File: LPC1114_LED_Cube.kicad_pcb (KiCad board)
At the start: 2 copper layers, 100 x 100 mm, 88 parts, among them Q201 BSS138, Q202 BSS138, Q203 BSS138, Q204 BSS138, Q205 IRLML6402TRPBF, Q206 IRLML6402TRPBF, Q207 IRLML6402TRPBF, Q208 IRLML6402TRPBF, Q209 BSS138, Q210 BSS138, Q211 BSS138, Q212 BSS138, Q213 IRLML6402TRPBF, Q214 IRLML6402TRPBF, Q215 IRLML6402TRPBF, Q216 IRLML6402TRPBF, Y101 12MHZ, Y102 12MHZ

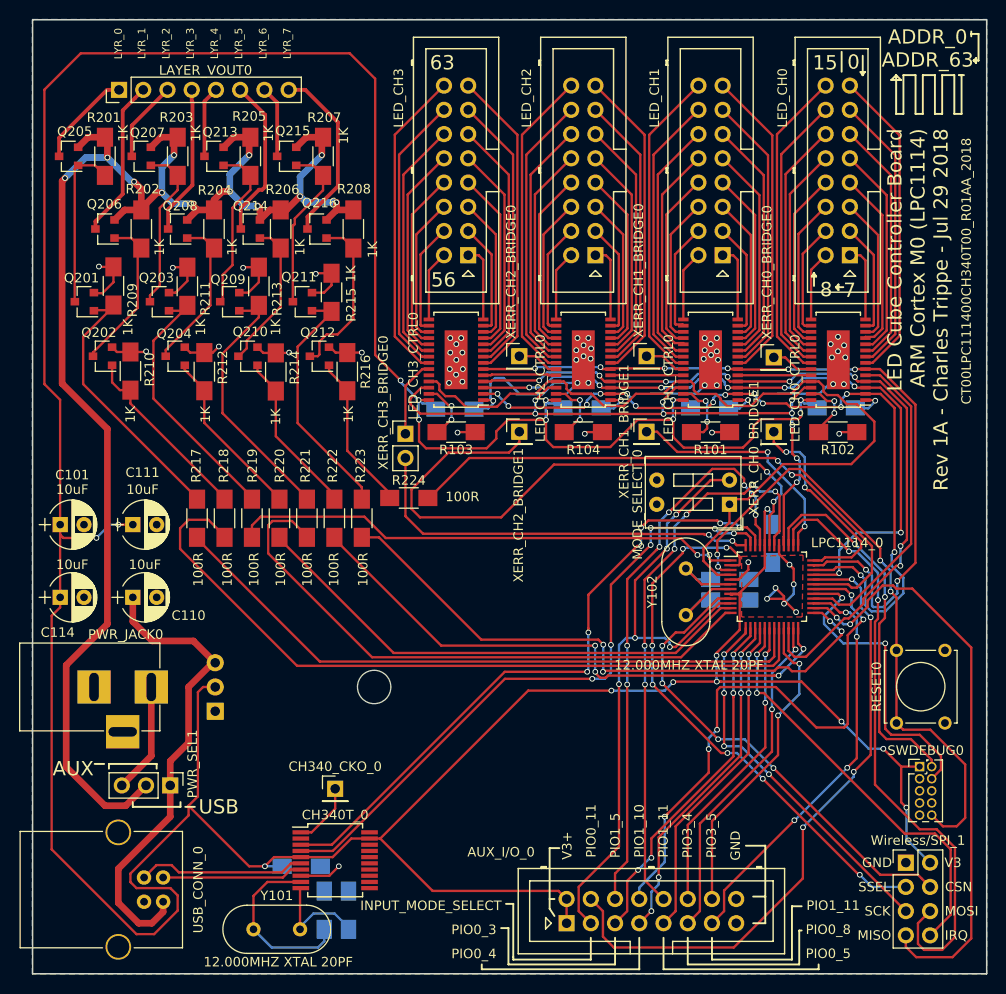
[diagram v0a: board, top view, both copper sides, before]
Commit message: Rev 1B: Corrected silkscreen component values
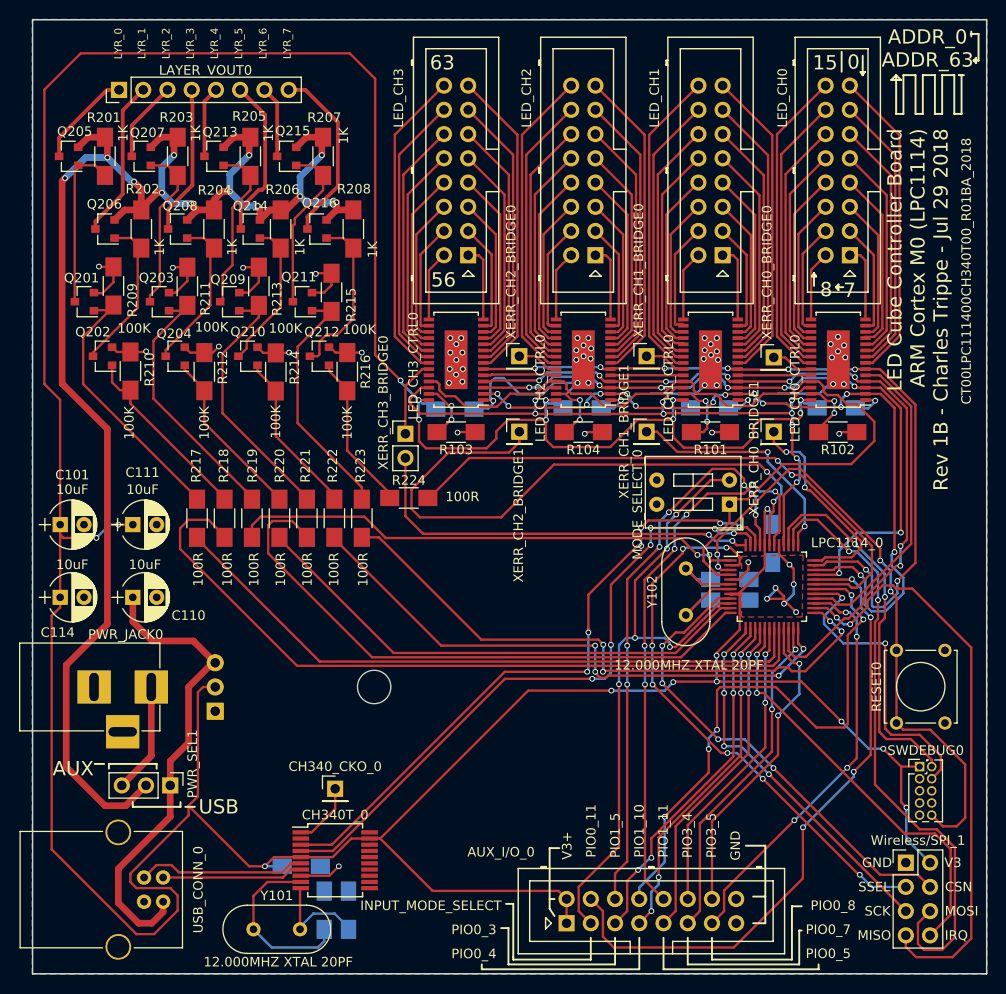
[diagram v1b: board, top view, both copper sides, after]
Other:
- board text added: "100K"
- board text added: "22pF"
- board text added: "CT00LPC111400CH340T00_R01BA_2018"
- board text added: "LED Cube Controller Board ARM Cortex M0 (LPC1114) Rev 1B - Charles Trippe - Jul 29 2018"
- board text added: "PIO0_7"
- board text removed: "CT00LPC111400CH340T00_R01AA_2018"
- board text removed: "LED Cube Controller Board ARM Cortex M0 (LPC1114) Rev 1A - Charles Trippe - Jul 29 2018"
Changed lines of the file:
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@@
   (layers
     (0 F.Cu signal)
-    (31 B.Cu signal)
+    (31 B.Cu signal hide)
     (32 B.Adhes user hide)
     (33 F.Adhes user hide)
     (34 B.Paste user hide)
     (35 F.Paste user hide)
-    (36 B.SilkS user)
+    (36 B.SilkS user hide)
     (37 F.SilkS user)
-    (38 B.Mask user)
-    (39 F.Mask user)
+    (38 B.Mask user hide)
+    (39 F.Mask user hide)
     (40 Dwgs.User user hide)
     (41 Cmts.User user hide)
@@
     (tags SOT-23)
     (attr smd)
-    (fp_text reference Q202 (at 0.38354 2.48158 180) (layer F.SilkS)
+    (fp_text reference Q202 (at 1.016 2.54 180) (layer F.SilkS)
       (effects (font (size 1 1) (thickness 0.15)))
     )
@@
     (tags SOT-23)
     (attr smd)
-    (fp_text reference Q210 (at -0.2413 2.56286 180) (layer F.SilkS)
+    (fp_text reference Q210 (at 0 2.56286 180) (layer F.SilkS)
       (effects (font (size 1 1) (thickness 0.15)))
     )
@@
     (tags SOT-23)
     (attr smd)
-    (fp_text reference Q212 (at 0.1778 2.48158 180) (layer F.SilkS)
+    (fp_text reference Q212 (at -0.254 2.54 180) (layer F.SilkS)
       (effects (font (size 1 1) (thickness 0.15)))
     )
@@
     )
   )
+  (gr_text 100K (at 119.253 77.47) (layer F.SilkS)
+    (effects (font (size 1 1) (thickness 0.2)))
+  )
+  (gr_text 100K (at 111.506 77.343) (layer F.SilkS)
+    (effects (font (size 1 1) (thickness 0.2)))
+  )
+  (gr_text 100K (at 103.759 77.216) (layer F.SilkS)
+    (effects (font (size 1 1) (thickness 0.2)))
+  )
+  (gr_text 100K (at 95.631 77.343) (layer F.SilkS)
+    (effects (font (size 1 1) (thickness 0.2)))
+  )
   (gr_line (start 152.273 105.029) (end 154.305 105.029) (layer B.SilkS) (width 0.2))
   (gr_line (start 152.4 104.013) (end 154.305 104.013) (layer B.SilkS) (width 0.2))
@@
     (effects (font (size 1 1) (thickness 0.2)) (justify mirror))
   )
-  (gr_text 0.1uF (at 113.284 137.16 90) (layer B.SilkS)
+  (gr_text 22pF (at 113.284 137.16 90) (layer B.SilkS)
     (effects (font (size 1 1) (thickness 0.2)) (justify mirror))
   )
@@
     (effects (font (size 1 1) (thickness 0.2)) (justify mirror))
   )
-  (gr_text 0.1uF (at 121.793 139.446 90) (layer B.SilkS)
+  (gr_text 22pF (at 121.793 139.446 90) (layer B.SilkS)
     (effects (font (size 1 1) (thickness 0.2)) (justify mirror))
   )
@@
   (gr_poly (pts (xy 154.432 81.153) (xy 154.432 77.343) (xy 157.607 77.343) (xy 157.607 81.153)) (layer B.Mask) (width 0.15))
   (gr_poly (pts (xy 167.894 81.153) (xy 167.894 77.343) (xy 171.069 77.343) (xy 171.069 81.153)) (layer B.Mask) (width 0.15))
-  (gr_text CT00LPC111400CH340T00_R01AA_2018 (at 182.88 71.345143 90) (layer F.SilkS)
+  (gr_text CT00LPC111400CH340T00_R01BA_2018 (at 182.88 71.345143 90) (layer F.SilkS)
     (effects (font (size 1 1) (thickness 0.2)))
   )
-  (gr_text "LED Cube Controller Board\nARM Cortex M0 (LPC1114)\nRev 1A - Charles Trippe - Jul 29 2018" (at 177.8 56.388 90) (layer F.SilkS)
+  (gr_text "LED Cube Controller Board\nARM Cortex M0 (LPC1114)\nRev 1B - Charles Trippe - Jul 29 2018" (at 177.8 56.388 90) (layer F.SilkS)
     (effects (font (size 1.5 1.5) (thickness 0.3)) (justify right))
   )
@@
     (effects (font (size 1 1) (thickness 0.2)))
   )
-  (gr_text 1K (at 118.364 71.628 90) (layer F.SilkS)
-    (effects (font (size 1 1) (thickness 0.2)))
-  )
-  (gr_text 1K (at 110.49 77.216 90) (layer F.SilkS)
-    (effects (font (size 1 1) (thickness 0.2)))
-  )
-  (gr_text 1K (at 102.616 77.216 90) (layer F.SilkS)
-    (effects (font (size 1 1) (thickness 0.2)))
-  )
-  (gr_text 1K (at 94.996 77.216 90) (layer F.SilkS)
-    (effects (font (size 1 1) (thickness 0.2)))
-  )
   (gr_text 1K (at 98.298 68.834 90) (layer F.SilkS)
     (effects (font (size 1 1) (thickness 0.2)))
@@
     (effects (font (size 1 1) (thickness 0.2)))
   )
-  (gr_text 1K (at 118.11 86.36 90) (layer F.SilkS)
+  (gr_text 100K (at 117.983 87.249 90) (layer F.SilkS)
     (effects (font (size 1 1) (thickness 0.2)))
   )
-  (gr_text 1K (at 110.49 86.614 90) (layer F.SilkS)
+  (gr_text 100K (at 110.49 87.122 90) (layer F.SilkS)
     (effects (font (size 1 1) (thickness 0.2)))
   )
-  (gr_text 1K (at 103.124 86.36 90) (layer F.SilkS)
+  (gr_text 100K (at 102.997 87.249 90) (layer F.SilkS)
     (effects (font (size 1 1) (thickness 0.2)))
   )
-  (gr_text 1K (at 95.25 86.36 90) (layer F.SilkS)
+  (gr_text 100K (at 95.123 87.249 90) (layer F.SilkS)
     (effects (font (size 1 1) (thickness 0.2)))
   )
@@
     (effects (font (size 1 1) (thickness 0.2)))
   )
-  (gr_text PIO0_8 (at 168.402 140.360035) (layer F.SilkS)
+  (gr_text PIO0_7 (at 168.402 140.360035) (layer F.SilkS)
     (effects (font (size 1 1) (thickness 0.2)))
   )
@@
     (effects (font (size 1 1) (thickness 0.2)))
   )
-  (gr_text PIO1_11 (at 168.91 137.838904) (layer F.SilkS)
+  (gr_text PIO0_8 (at 168.91 137.838904) (layer F.SilkS)
     (effects (font (size 1 1) (thickness 0.2)))
   )
